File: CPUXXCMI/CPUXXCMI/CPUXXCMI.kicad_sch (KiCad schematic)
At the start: 68 parts, among them J1 BUS, J2 UART, U1 74HC245, U10 MC6850, U11 MAX233, U12 4040, U13 GAL22V10, U14 GAL16V8, U15 74LS74, U16 74LS74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

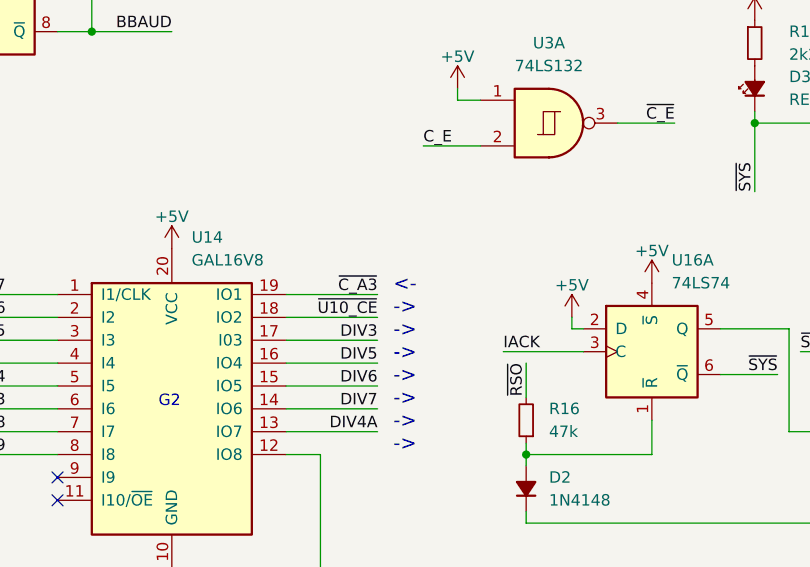
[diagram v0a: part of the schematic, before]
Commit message: Exorciser Doku added
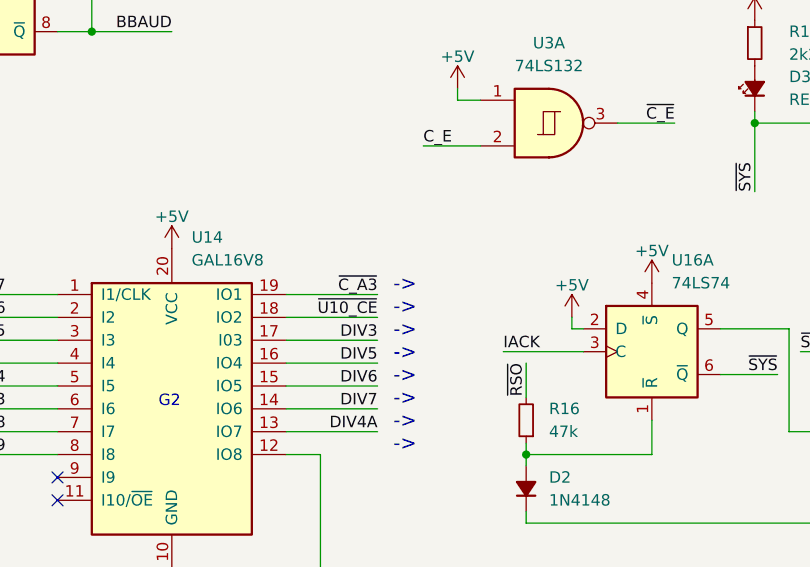
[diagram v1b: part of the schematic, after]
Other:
- note added: "-> -> -> -> -> -> -> ->"
- note removed: "<- -> -> -> -> -> -> ->"
